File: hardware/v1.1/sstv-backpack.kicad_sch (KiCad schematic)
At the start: 21 parts, among them J1 Conn_01x03_Pin, J2 Conn_01x02_Pin, J3 2172034-1, SW1 SW_Push, SW2 SLW-1276864-4A-D, U1 ESP32-CAM, U2 FT231XS

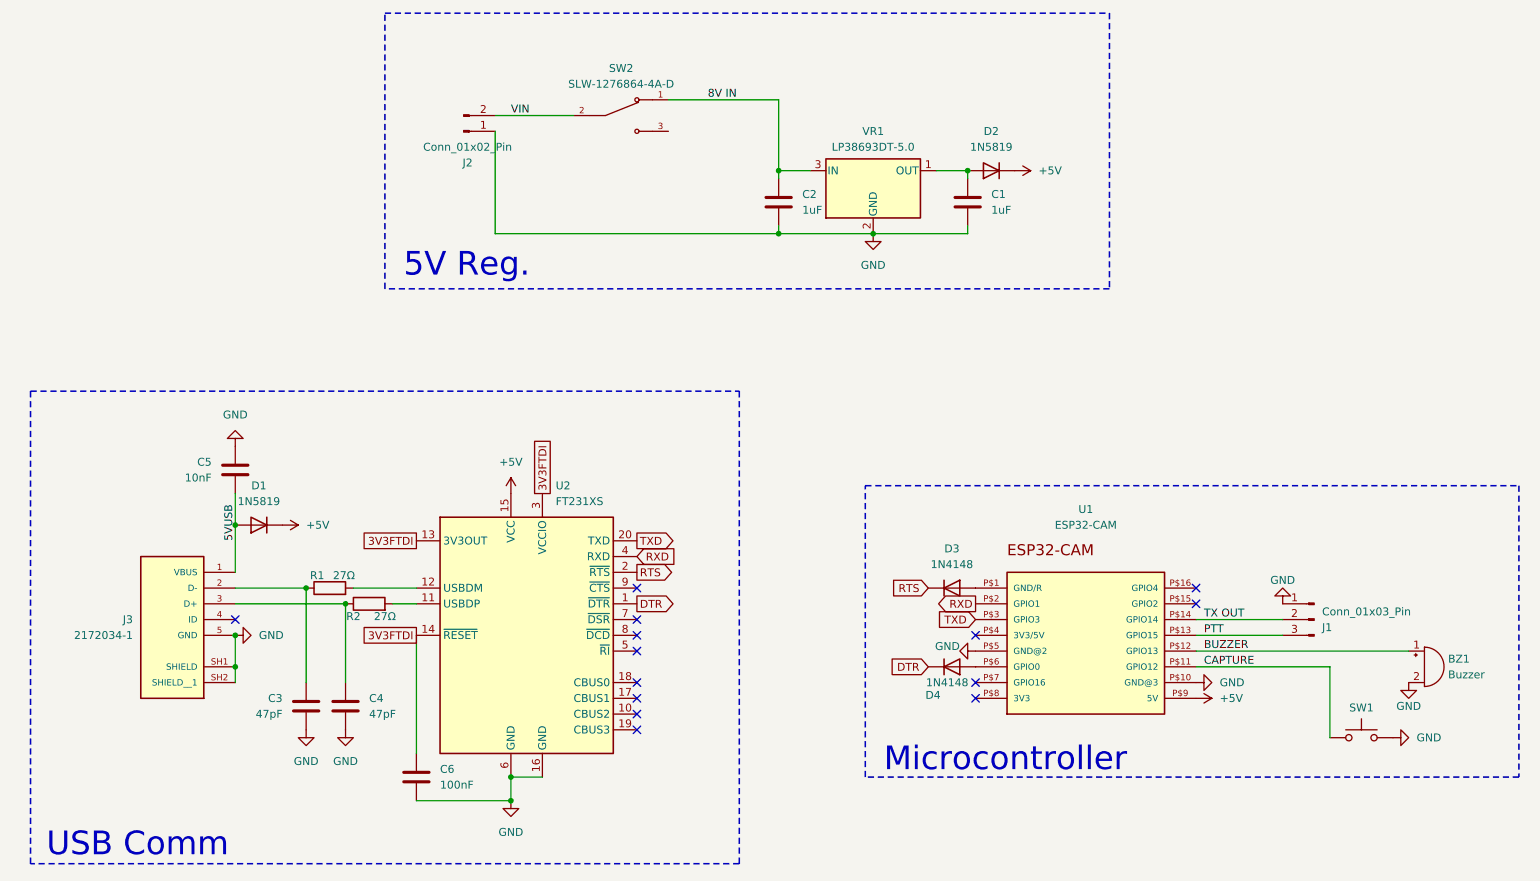
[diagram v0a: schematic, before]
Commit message: Swap v1.1 to USB-C and add v1.2
Swapped v1.1 to USB-C from USB Mini B, added the TX transmit transistor to hopefully fix the TX hang, and added the WIP files for v1.2
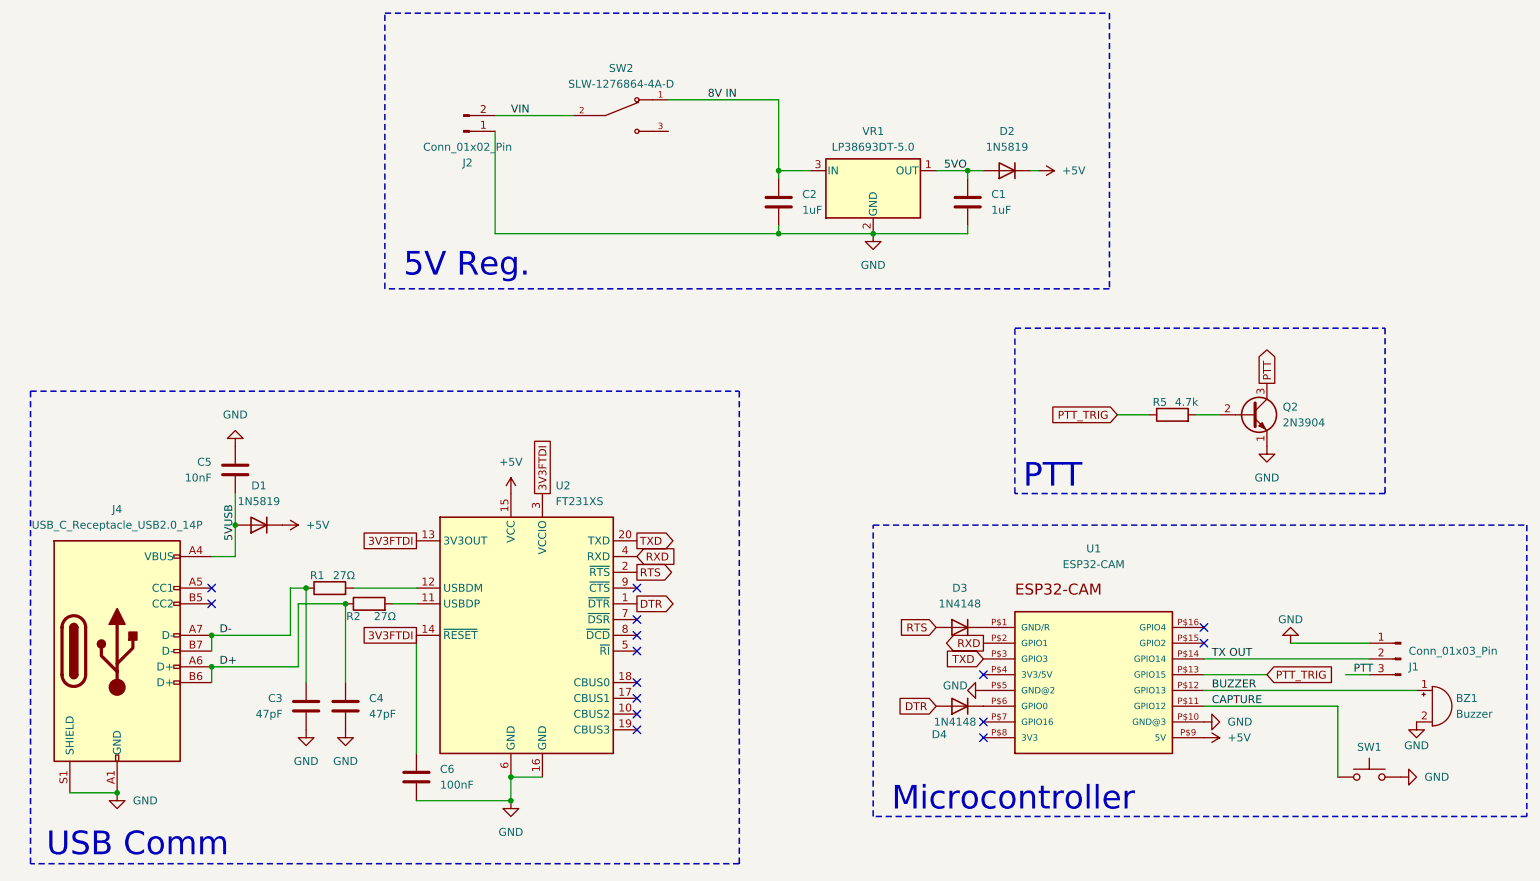
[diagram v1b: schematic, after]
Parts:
- removed J3: 2172034-1, 2172034-1:TE_2172034-1, symbol 2172034-1:2172034-1
- added J4: USB_C_Receptacle_USB2.0_14P, Connector_USB:USB_C_Receptacle_GCT_USB4085, symbol Connector:USB_C_Receptacle_USB2.0_14P
- added Q2: 2N3904, Package_TO_SOT_THT:TO-92_Inline, symbol Transistor_BJT:2N3904
- added R5: 4.7k, Resistor_THT:R_Axial_DIN0207_L6.3mm_D2.5mm_P7.62mm_Horizontal, symbol Device:R
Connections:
- net 5VUSB: now also J4.A4 (VBUS), J4.A9 (VBUS), J4.B4 (VBUS), J4.B9 (VBUS)
- net DTR: now also D4.2 (A); no longer D4.1 (K)
- net GND: now also J4.A1 (GND), J4.A12 (GND), J4.B1 (GND), J4.B12 (GND), J4.S1 (SHIELD), Q2.1 (E)
- net PTT: now also Q2.3 (C); no longer U1.P$13 (GPIO15)
- net RTS: now also D3.2 (A); no longer D3.1 (K)
- net D+: now reaches C4.1, R2.1
- net D+: now also J4.A6 (D+), J4.B6 (D+)
- net 5VO: now reaches C1.1, D2.2 (A), VR1.1 (OUT)
- net D-: now reaches C3.1, R1.1
- net D-: now also J4.A7 (D-), J4.B7 (D-)
- net at U1.P$1 (GND/R): now also D3.1 (K); no longer D3.2 (A)
- net at U1.P$6 (GPIO0): now also D4.1 (K); no longer D4.2 (A)
- new net: Q2.2 (B), R5.2
- new net PTT_TRIG: R5.1, U1.P$13 (GPIO15)
- no-connect marks 14 -> 15
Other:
- note added: "PTT"
- moved on the sheet: BZ1, D2, D3, D4, J1, SW1, U1

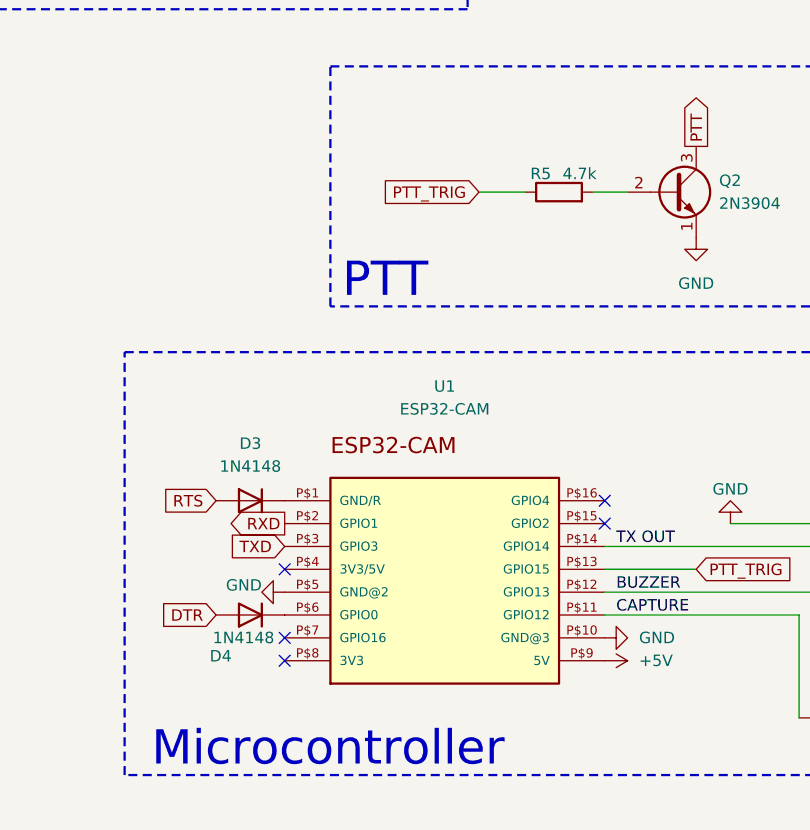
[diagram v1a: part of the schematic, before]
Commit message: Fix PCB and add USB-C to case
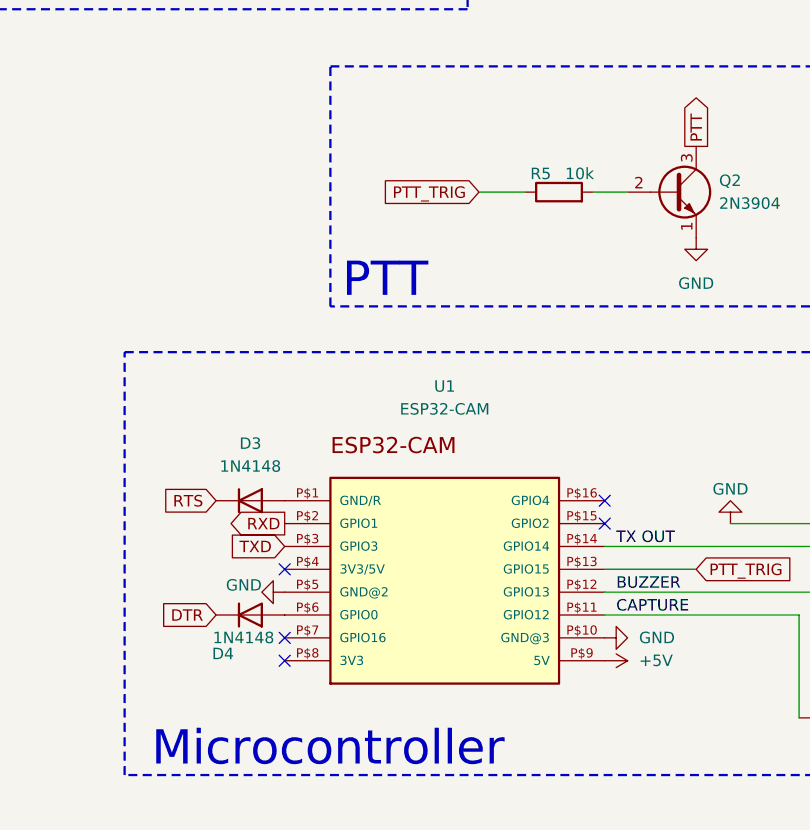
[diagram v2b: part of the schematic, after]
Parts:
- R5: value 4.7k -> 10k
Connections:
- net DTR: now also D4.1 (K); no longer D4.2 (A)
- net RTS: now also D3.1 (K); no longer D3.2 (A)
- net at U1.P$1 (GND/R): now also D3.2 (A); no longer D3.1 (K)
- net at U1.P$6 (GPIO0): now also D4.2 (A); no longer D4.1 (K)
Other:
- moved on the sheet: D4
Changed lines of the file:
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@@
 			)
 		)
-		(property "Value" "4.7k"
+		(property "Value" "10k"
 			(at 214.376 89.408 90)
 			(effects
@@
 		(lib_id "Device:D")
 		(at 177.8 125.73 0)
-		(mirror y)
 		(unit 1)
 		(exclude_from_sim no)
@@
 	(symbol
 		(lib_id "Device:D")
-		(at 177.8 138.43 180)
+		(at 177.8 138.43 0)
+		(mirror x)
 		(unit 1)
 		(exclude_from_sim no)
@@
 		(dnp no)
 		(property "Reference" "D4"
-			(at 174.498 143.002 0)
-			(effects
-				(font
+			(at 174.752 142.748 0)
+			(effects
+				(font
